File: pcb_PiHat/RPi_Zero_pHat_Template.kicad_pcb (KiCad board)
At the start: 2 copper layers, 65 x 30 mm, 7 parts, among them J1 RPi_GPIO, J2 Isolated_ISP, J3 Isolated_ISP

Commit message: pcb_PiHat: Relee headeri lisätty
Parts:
- added J4: Conn_Relay, Pin_Headers:Pin_Header_Straight_1x03_Pitch2.54mm, F.Cu at (21.1, 36.3)
- moved J2 10.7 mm to (31.5, 36.2)
- moved J3 10.7 mm to (31.5, 43.6)
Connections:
- J1 pad 16: (no net) -> Net-(J1-Pad16)
- J1 pad 2: (no net) -> Net-(J1-Pad2)
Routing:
- net Net-(J1-Pad16): track 0.00 -> 23.7 mm
- net Net-(J1-Pad21): track 40.4 -> 18.3 mm
- net Net-(J1-Pad23): track 27.3 -> 42.7 mm
- net Net-(J1-Pad40): track 56.2 -> 42.6 mm
- net Net-(J1-Pad22): track 49.4 -> 35.8 mm
- net Net-(J1-Pad38): track 49.0 -> 36.5 mm
- net Net-(J1-Pad2): track 0.00 -> 10.7 mm
- net Net-(J1-Pad29): track 30.4 -> 19.9 mm
- net +3V3: track 15.2 -> 25.1 mm
- net Net-(J1-Pad24): track 20.1 -> 10.3 mm
- net Net-(J1-Pad19): track 18.1 -> 9.60 mm
- net Net-(J1-Pad35): track 65.4 -> 60.1 mm
- net Net-(J1-Pad11): track 27.0 -> 32.2 mm

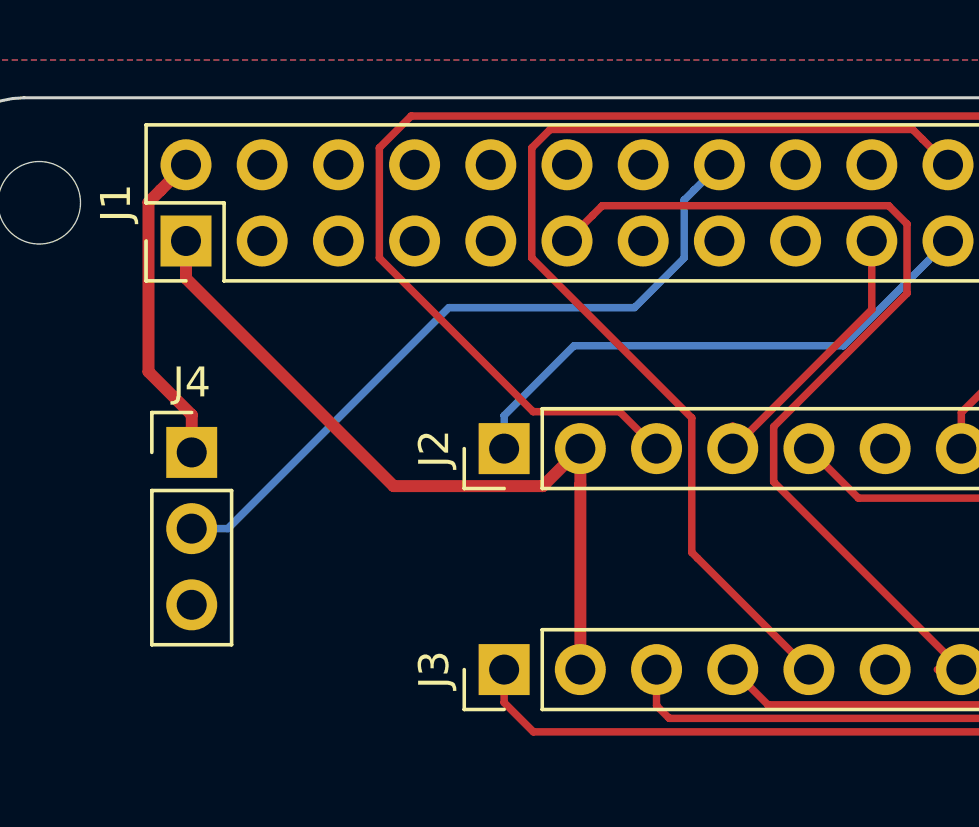
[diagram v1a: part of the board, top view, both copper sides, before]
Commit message: pcb_PiHat: Toisen releen headeri lisätty
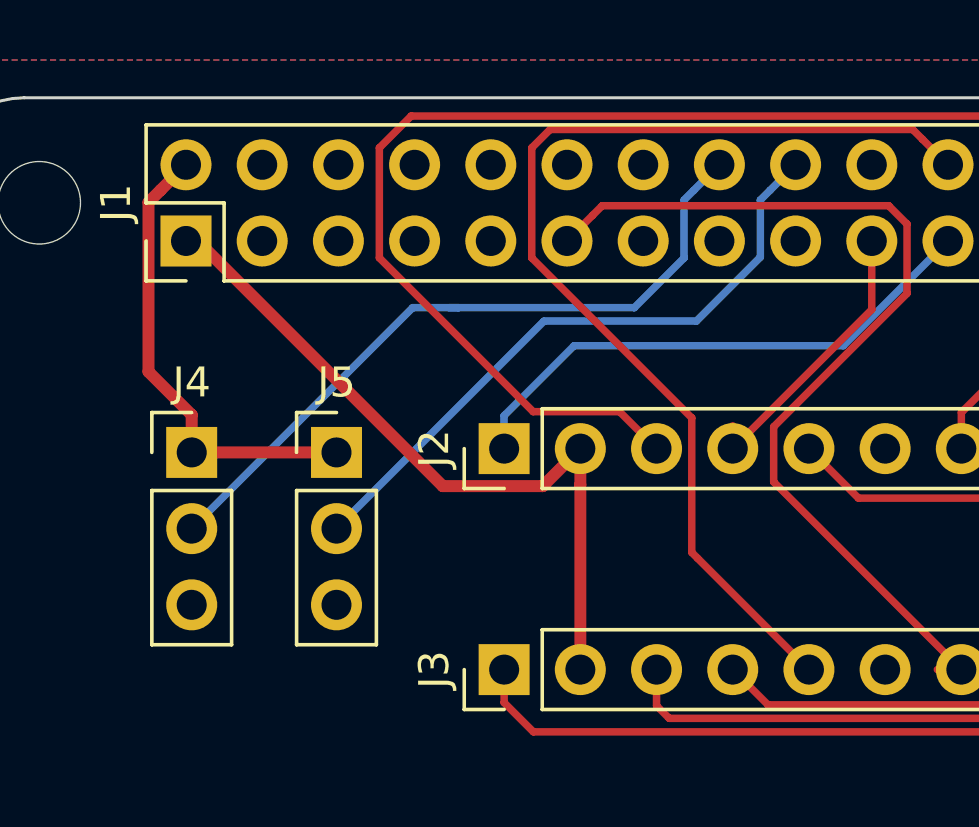
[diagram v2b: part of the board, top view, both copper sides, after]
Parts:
- added J5: Conn_Relay, Connector_PinHeader_2.54mm:PinHeader_1x03_P2.54mm_Vertical, F.Cu at (25.9, 36.3)
- J1: footprint Pin_Headers:Pin_Header_Straight_2x20_Pitch2.54mm -> Connector_PinHeader_2.54mm:PinHeader_2x20_P2.54mm_Vertical
- J2, J3: footprint Pin_Headers:Pin_Header_Straight_1x08_Pitch2.54mm -> Connector_PinHeader_2.54mm:PinHeader_1x08_P2.54mm_Vertical
- J4: footprint Pin_Headers:Pin_Header_Straight_1x03_Pitch2.54mm -> Connector_PinHeader_2.54mm:PinHeader_1x03_P2.54mm_Vertical
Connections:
- J1 pad 10: (no net) -> Net-(J1-Pad10)
- J1 pad 12: (no net) -> Net-(J1-Pad12)
- J1 pad 13: (no net) -> Net-(J1-Pad13)
- J1 pad 15: (no net) -> Net-(J1-Pad15)
- J1 pad 17: (no net) -> Net-(J1-Pad17)
- J1 pad 18: (no net) -> Net-(J1-Pad18)
- J1 pad 26: (no net) -> Net-(J1-Pad26)
- J1 pad 27: (no net) -> Net-(J1-Pad27)
- J1 pad 28: (no net) -> Net-(J1-Pad28)
- J1 pad 3: (no net) -> Net-(J1-Pad3)
- J1 pad 31: (no net) -> Net-(J1-Pad31)
- J1 pad 32: (no net) -> Net-(J1-Pad32)
- J1 pad 33: (no net) -> Net-(J1-Pad33)
- J1 pad 36: (no net) -> Net-(J1-Pad36)
- J1 pad 37: (no net) -> Net-(J1-Pad37)
- J1 pad 4: (no net) -> Net-(J1-Pad4)
- J1 pad 5: (no net) -> Net-(J1-Pad5)
- J1 pad 7: (no net) -> Net-(J1-Pad7)
- J1 pad 8: (no net) -> Net-(J1-Pad8)
- J2 pad 8: (no net) -> Net-(J2-Pad8)
- J3 pad 8: (no net) -> Net-(J3-Pad8)
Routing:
- net Net-(J1-Pad18): track 0.00 -> 21.4 mm
- net Net-(J1-Pad2): track 10.7 -> 15.5 mm
- net +3V3: track 25.1 -> 24.4 mm

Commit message: raspi hat toteutettu versio
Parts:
- added J10: USB_A, Connectors:USB_A, F.Cu at (46.8, 52.3)
- added J6: Conn_01x03, Pin_Headers:Pin_Header_Straight_1x03_Pitch2.54mm, F.Cu at (44.1, 48.9)
- added J7: Conn_switch, Pin_Headers:Pin_Header_Straight_1x02_Pitch2.54mm, F.Cu at (70.0, 42.3)
- added J8: Conn_switch, Pin_Headers:Pin_Header_Straight_1x02_Pitch2.54mm, F.Cu at (73.6, 42.3)
- added J9: 5V_in, 5V_power:5V_power, F.Cu at (63.6, 48.4)
- added Q1: Q_NPN_EBC, TO_SOT_Packages_THT:TO-92_Inline_Wide, F.Cu at (18.5, 41.0)
- added R1: R, Resistors_THT:R_Axial_DIN0207_L6.3mm_D2.5mm_P10.16mm_Horizontal, F.Cu at (28.5, 35.0)
- added U1: SPUN02L-12, SPUN02L-12:SPUN02L-12, F.Cu at (23.2, 49.9)
- moved J4 13.0 mm to (34.1, 35.3)
- moved J5 13.0 mm to (38.9, 35.3)
- moved J2 12.5 mm to (44.0, 35.2)
- moved J3 12.5 mm to (44.0, 42.6)
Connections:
- J1 pad 1: +3V3 -> Net-(J1-Pad1)
- J2 pad 2: +3V3 -> Net-(J1-Pad2)
- J3 pad 2: +3V3 -> Net-(J1-Pad2)
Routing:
- net GND: track 0.00 -> 259.9 mm
- net Net-(J1-Pad2): track 15.5 -> 172.6 mm
- net Net-(J1-Pad5): track 0.00 -> 84.0 mm, vias 0 -> 2
- net Net-(J6-Pad1): track 0.00 -> 41.0 mm
- net Net-(J1-Pad23): track 42.7 -> 6.02 mm
- net Net-(J1-Pad36): track 0.00 -> 27.0 mm
- net Net-(J1-Pad12): track 0.00 -> 25.8 mm
- net +3V3: track 24.4 -> 0.00 mm
- net Net-(J1-Pad35): track 60.1 -> 41.7 mm
- net Net-(J1-Pad11): track 32.2 -> 48.3 mm
- net Net-(J1-Pad29): track 19.9 -> 6.87 mm
- net Net-(J1-Pad21): track 18.3 -> 6.87 mm
- net Net-(Q1-Pad2): track 0.00 -> 10.8 mm
- net Net-(J6-Pad2): track 0.00 -> 9.86 mm
- net Net-(J1-Pad18): track 21.4 -> 14.0 mm
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- removed copper zone on F.Cu, net GND
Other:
- board outline removed
- net class Default: clearance 0.2 -> 0.25; trace_width 0.25 -> 0.3; via_dia 0.6 -> 2; via_drill 0.4 -> 1
- rule trace_clearance: 0.2 -> 0.25
